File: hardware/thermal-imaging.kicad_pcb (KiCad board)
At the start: 2 copper layers, 40 x 40 mm, 47 parts, among them P1 CON-SENSOR, P2 Boot, Q1 Oscillator, U1 XMC1XXX24, U10 DRILL, U11 DRILL, U2 74LVC1G17, U3 74LVC1G17, U4 FLIR-Lepton, U5 AP7333-28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

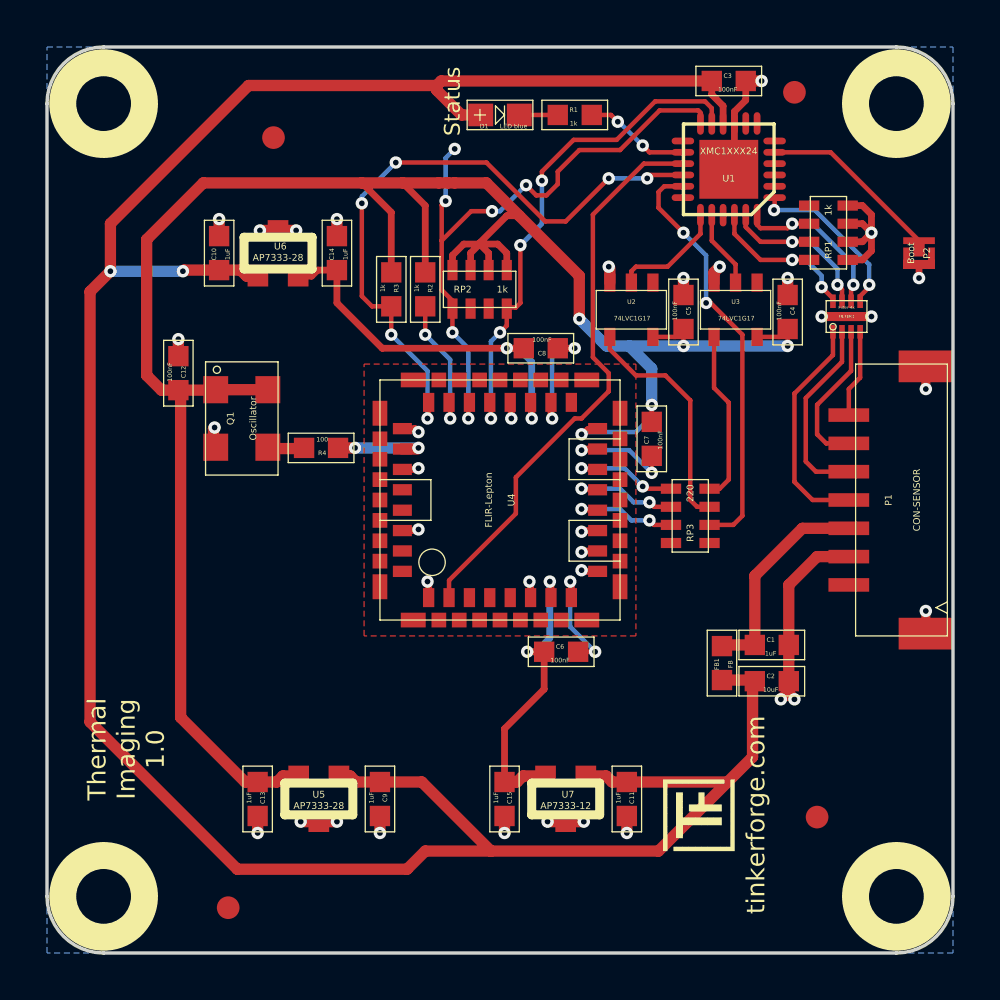
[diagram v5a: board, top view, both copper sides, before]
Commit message: fix vsync connection, footprints
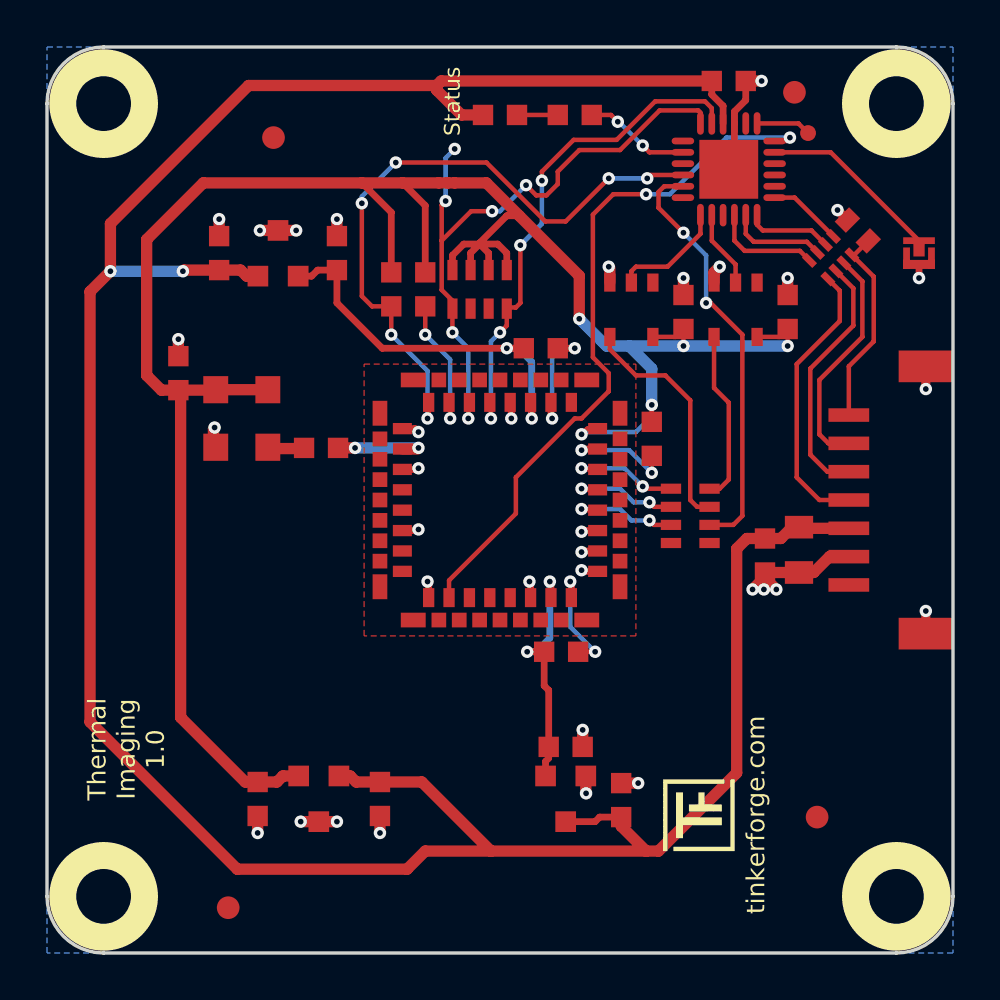
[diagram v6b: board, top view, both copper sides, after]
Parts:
- removed FB1: FB, kicad-libraries:0603F
- removed FILTER1: Filter-4x, kicad-libraries:DFN8-17x135
- added C16: TBD, C0402E, F.Cu at (202.2, 89.0)
- added P3: Debug, DEBUG_PAD, F.Cu at (200.0, 84.7)
- C1: value 1uF -> 10uF; footprint kicad-libraries:0603F -> kicad-libraries:C0805
- C10, C11, C12, C13, C14, C15, C3, C4, C5, C6, C7, C8, C9: footprint kicad-libraries:0603F -> kicad-libraries:C0603F
- C2: value 10uF -> 1uF; footprint kicad-libraries:0603F -> kicad-libraries:C0603F
- D1: footprint kicad-libraries:D0603E -> kicad-libraries:D0603F
- R1, R2, R3, R4: footprint 0603F -> kicad-libraries:R0603F
- RP1: value 1k -> TBD; footprint 0603X4 -> kicad-libraries:4X0402
- RP2, RP3: footprint 0603X4 -> kicad-libraries:0603X4
- U2, U3: footprint SOT23-5 -> kicad-libraries:SOT23-5
- U4: footprint Lepton_105028 -> kicad-libraries:Lepton_105028
- U5, U6: footprint SOT23-3 -> kicad-libraries:SOT23-3
- U7: footprint SOT23-3 -> kicad-libraries:SOT23-3R
- moved C2 5.56 mm to (198.1, 103.3), turned to 90 degrees
- moved C1 4.37 mm to (199.6, 103.1), turned to 90 degrees
- moved C15 3.55 mm to (189.3, 111.8), turned to 180 degrees
- moved RP1 1.10 mm to (201.0, 90.2), turned to 225 degrees
- moved C11 0.25 mm to (191.8, 114.2), turned to 270 degrees
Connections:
- C1 pad 2: Net-(C1-Pad2) -> 3V3
- P1 pad 3: Net-(C1-Pad2) -> 3V3
- P1 pad 4: Net-(FILTER1-Pad1) -> Net-(P1-Pad4)
- P1 pad 5: Net-(FILTER1-Pad2) -> Net-(P1-Pad5)
- P1 pad 6: Net-(FILTER1-Pad3) -> Net-(P1-Pad6)
- P1 pad 7: Net-(FILTER1-Pad4) -> Net-(C16-Pad2)
- RP1 pad 1: (no net) -> S-MISO
- RP1 pad 5: GND -> Net-(P1-Pad4)
- RP1 pad 6: GND -> Net-(P1-Pad5)
- RP1 pad 7: GND -> Net-(P1-Pad6)
- RP1 pad 8: GND -> Net-(C16-Pad2)
- U1 pad 15: VSYNC -> (no net)
- U1 pad 6: (no net) -> VSYNC
- U1 pad 7: (no net) -> Net-(P3-Pad1)
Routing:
- net Net-(P1-Pad4): track 0.00 -> 12.5 mm
- net GND: track 65.8 -> 54.4 mm, vias 42 -> 40
- net Net-(P1-Pad5): track 0.00 -> 11.2 mm
- net Net-(P1-Pad6): track 0.00 -> 10.2 mm
- net Net-(FILTER1-Pad1): track 10.1 -> 0.00 mm
- net Net-(C1-Pad2): track 9.54 -> 0.00 mm
- net Net-(C16-Pad2): track 0.00 -> 8.91 mm
- net Net-(FILTER1-Pad2): track 8.47 -> 0.00 mm
- net 3V3: track 116.1 -> 123.7 mm
- net Net-(FILTER1-Pad3): track 6.71 -> 0.00 mm
- net VSYNC: track 25.2 -> 31.1 mm, vias 0 -> 2
- net S-MISO: track 7.55 -> 3.31 mm, vias 2 -> 0
- net S-MOSI: track 7.98 -> 3.80 mm, vias 2 -> 0
- net Net-(FILTER1-Pad4): track 3.88 -> 0.00 mm
- net S-CLK: track 7.60 -> 4.33 mm, vias 2 -> 0
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
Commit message: fix part texts
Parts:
- U7: value AP7333-12 -> MCP1700T-1202E/TT
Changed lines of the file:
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@@
-(kicad_pcb (version 4) (host pcbnew 4.0.2+e4-6225~38~ubuntu15.10.1-stable)
+(kicad_pcb (version 4) (host pcbnew 4.0.6-e0-6349~53~ubuntu16.04.1)
   (general
     (links 145)
     (no_connects 0)
-    (area 165.544999 80.044999 282.44286 160.84)
+    (area 165.544999 80.044999 282.34286 161.24)
     (thickness 1.6)
     (drawings 12)
@@
   (layers
     (0 F.Cu signal)
-    (31 B.Cu signal)
+    (31 B.Cu signal hide)
     (32 B.Adhes user hide)
     (33 F.Adhes user hide)
@@
       (effects (font (size 0.3 0.3) (thickness 0.075)))
     )
-    (fp_text value AP7333-12 (at -0.05 -0.3) (layer F.Fab)
+    (fp_text value " MCP1700T-1202E/TT " (at -0.775 -1.15) (layer F.Fab)
       (effects (font (size 0.29972 0.29972) (thickness 0.07112)))
     )
@@
       (effects (font (size 0.3 0.3) (thickness 0.075)))
     )
-    (fp_text value AP7333-28 (at -0.65 -0.3) (layer F.Fab)
+    (fp_text value AP7333-28 (at 0.025 -0.3) (layer F.Fab)
       (effects (font (size 0.29972 0.29972) (thickness 0.07112)))
     )
@@
       (effects (font (size 0.3 0.3) (thickness 0.075)))
     )
-    (fp_text value AP7333-28 (at -0.65 -0.3 180) (layer F.Fab)
+    (fp_text value AP7333-28 (at -0.05 -0.275 180) (layer F.Fab)
       (effects (font (size 0.29972 0.29972) (thickness 0.07112)))
     )

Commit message: Fix CE logo
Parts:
- turned VAL to 0 degrees
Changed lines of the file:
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@@
-(kicad_pcb (version 4) (host pcbnew 4.0.6-e0-6349~53~ubuntu16.04.1)
+(kicad_pcb (version 4) (host pcbnew 4.0.2+dfsg1-stable)
   (general
     (links 145)
     (no_connects 0)
-    (area 165.544999 80.044999 282.34286 161.24)
+    (area 166.324999 80.824999 206.475001 120.975001)
     (thickness 1.6)
     (drawings 12)
@@
   )
   (module kicad-libraries:CE_5mm (layer B.Cu)
-    (at 178.4 100.9 180)
-    (fp_text reference VAL (at 0 0 180) (layer B.SilkS) hide
+    (at 178.4 100.9)
+    (fp_text reference VAL (at 0 0) (layer B.SilkS) hide
       (effects (font (size 1.143 1.143) (thickness 0.1778)) (justify mirror))
     )
-    (fp_text value CE_5mm (at 0 0 180) (layer B.SilkS) hide
+    (fp_text value CE_5mm (at 0 0) (layer B.SilkS) hide
       (effects (font (size 1.143 1.143) (thickness 0.1778)) (justify mirror))
     )
